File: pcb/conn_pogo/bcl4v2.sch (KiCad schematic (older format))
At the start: 3 parts

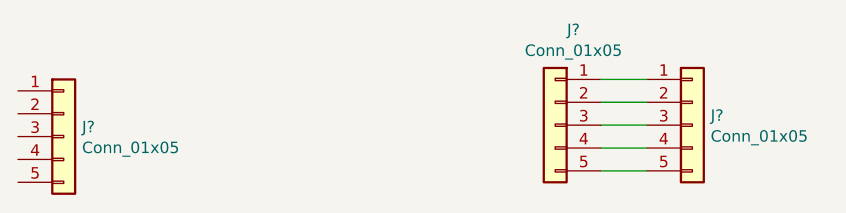
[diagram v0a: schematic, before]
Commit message: - make larger holes for pogo pins
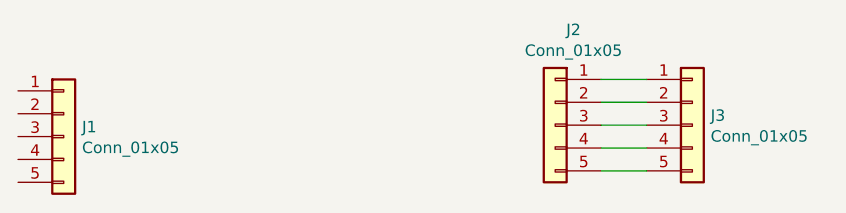
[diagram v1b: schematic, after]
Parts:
- J1: renamed from J?; footprint (none) -> libraries:5way_pogo_1.5mm_hole
- J2, J3: renamed from J?; footprint (none) -> libraries:5way_pogo_pad
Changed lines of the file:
@@
 $EndDescr
 $Comp
-L bcl4v2-rescue:Conn_01x05 J?
+L bcl4v2-rescue:Conn_01x05 J1
 U 1 1 5D1D2742
 P 5200 3000
-F 0 "J?" H 5280 3042 50  0000 L CNN
+F 0 "J1" H 5280 3042 50  0000 L CNN
 F 1 "Conn_01x05" H 5280 2951 50  0000 L CNN
-F 2 "" H 5200 3000 50  0001 C CNN
+F 2 "libraries:5way_pogo_1.5mm_hole" H 5200 3000 50  0001 C CNN
 F 3 "" H 5200 3000 50  0001 C CNN
 	1    5200 3000
@@
 $EndComp
 $Comp
-L bcl4v2-rescue:Conn_01x05 J?
+L bcl4v2-rescue:Conn_01x05 J2
 U 1 1 5D1D27C5
 P 7350 2950
-F 0 "J?" H 7270 3367 50  0000 C CNN
+F 0 "J2" H 7270 3367 50  0000 C CNN
 F 1 "Conn_01x05" H 7270 3276 50  0000 C CNN
-F 2 "" H 7350 2950 50  0001 C CNN
+F 2 "libraries:5way_pogo_pad" H 7350 2950 50  0001 C CNN
 F 3 "" H 7350 2950 50  0001 C CNN
 	1    7350 2950
@@
 $EndComp
 $Comp
-L bcl4v2-rescue:Conn_01x05 J?
+L bcl4v2-rescue:Conn_01x05 J3
 U 1 1 5D1D2841
 P 7950 2950
-F 0 "J?" H 8030 2992 50  0000 L CNN
+F 0 "J3" H 8030 2992 50  0000 L CNN
 F 1 "Conn_01x05" H 8030 2901 50  0000 L CNN
-F 2 "" H 7950 2950 50  0001 C CNN
+F 2 "libraries:5way_pogo_pad" H 7950 2950 50  0001 C CNN
 F 3 "" H 7950 2950 50  0001 C CNN
 	1    7950 2950
